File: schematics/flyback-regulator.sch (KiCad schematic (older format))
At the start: 24 parts

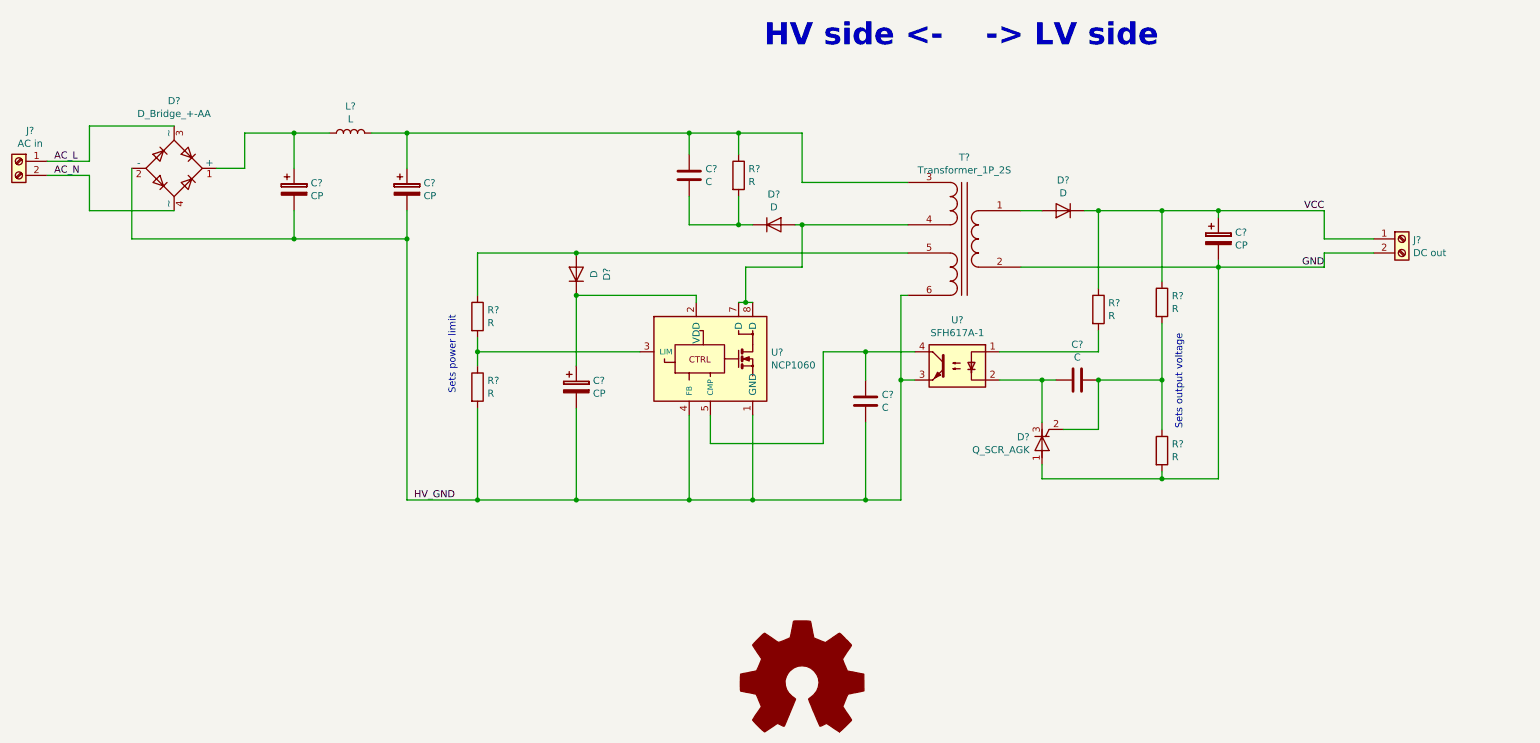
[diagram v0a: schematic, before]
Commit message: [sch] Edited to NCP1251
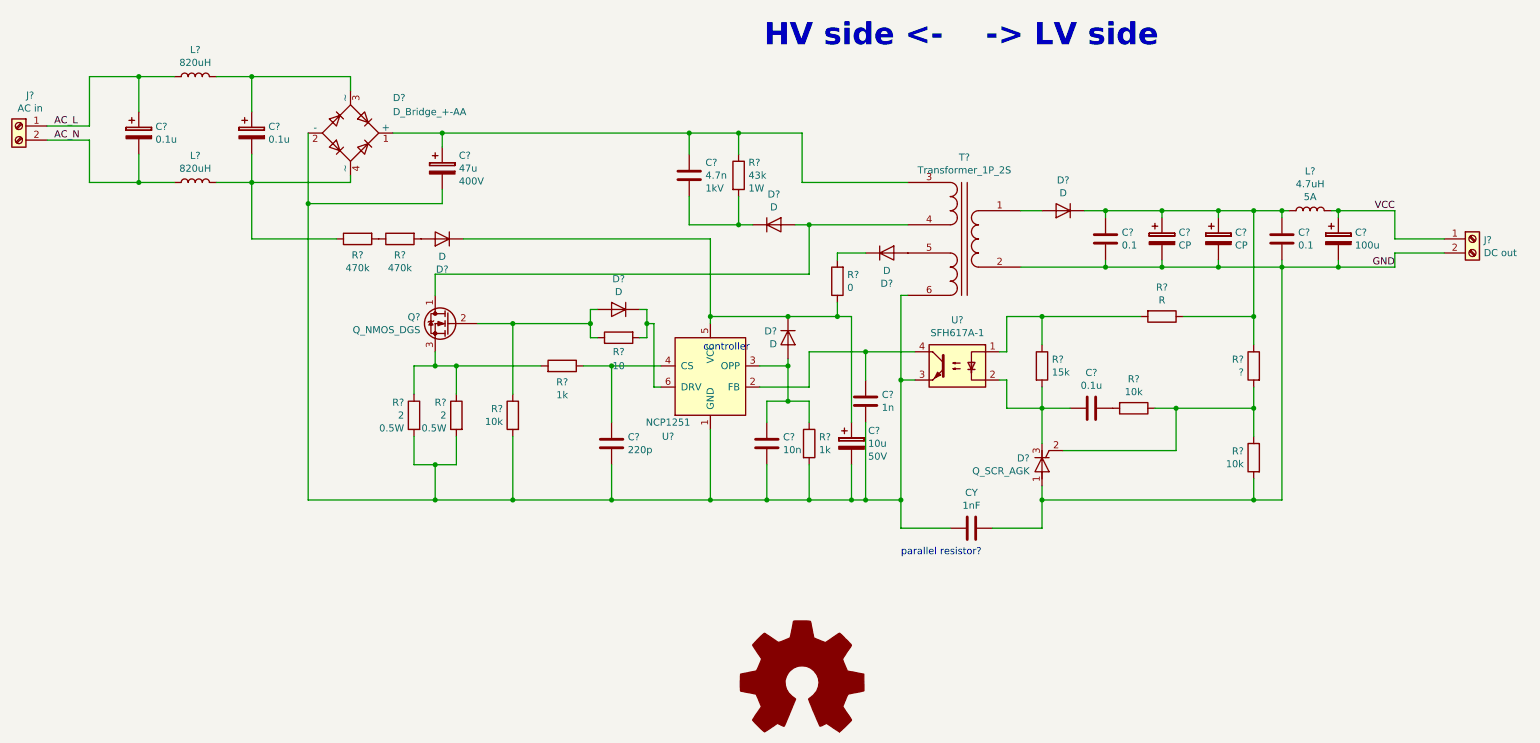
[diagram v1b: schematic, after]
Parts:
- removed C?: CP, symbol Device:CP
- removed R? (x4): R, symbol Device:R
- removed U?: NCP1060, Package_DIP:PowerIntegrations_PDIP-8B, symbol flyback-regulator-dedicated:NCP1060
- added C?: 47u, symbol Device:CP
- added C? (x2): 0.1, symbol Device:C
- added C?: CP, symbol Device:CP
- added C?: 100u, symbol Device:CP
- added C?: 10n, symbol Device:C
- added C?: 10u, symbol Device:CP
- added C?: 220p, symbol Device:C
- added CY: 1nF, symbol Device:C
- added D? (x3): D, symbol Device:D
- added L?: 820uH, symbol Device:L
- added L?: 4.7uH, symbol Device:L
- added Q?: Q_NMOS_DGS, symbol Device:Q_NMOS_DGS
- added R? (x2): 2, symbol Device:R
- added R? (x2): 10k, symbol Device:R
- added R?: 10, symbol Device:R
- added R? (x2): 470k, symbol Device:R
- added R?: R, symbol Device:R
- added R?: 15k, symbol Device:R
- added R?: ?, symbol Device:R
- added R? (x2): 1k, symbol Device:R
- added R?: 0, symbol Device:R
- added U?: NCP1251, symbol flyback-regulator-dedicated:NCP1251
- C? (x2): value CP -> 0.1u
- C?: value C -> 0.1u
- C?: value C -> 4.7n; Voltage (none) -> 1kV
- C?: value C -> 1n
- L?: value L -> 820uH
- R?: value R -> 10k
- R?: value R -> 43k; Power (none) -> 1W
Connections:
- net AC_L: now also C?.1, L?.1; no longer D?.3 (~~)
- net AC_N: now also C?.2, L?.1; no longer D?.4 (~~)
- net GND: now also C?.2, C?.2, C?.2, C?.2, CY.2, R?.2; no longer R?.2
- net VCC: now also C?.1, L?.2; no longer C?.1, D?.1 (K)
- net at C?.2, R?.1, T?.3 (SA): now also D?.1 (+), C?.1; no longer C?.1, L?.2
- net at D?.2 (A), T?.4 (SB): now also Q?.1 (D)
- net at U?.1: now also R?.1, R?.2
- net at C?.1, D?.3 (K), U?.2: now also R?.2
- net at C?.2, U?.4: now also U?.2 (FB)
- net at D?.2 (G), R?.1: now also R?.1, R?.2; no longer C?.2
- net at D?.1 (K): now also R?.2
- net HV_GND: no longer names the net of C?.1, D?.2 (-), T?.6 (SD), U?.3
- net HV_GND: now also C?.1, C?.1, C?.2, C?.2, CY.1, R?.2, R?.2, R?.2, R?.2, U?.1 (GND); no longer C?.2, C?.2
- new net: C?.1, D?.3 (~~), L?.2
- new net: C?.2, D?.4 (~~), L?.2, R?.1
- new net: C?.1, C?.1, C?.1, C?.1, D?.1 (K), L?.1, R?.1, R?.1
- new net: C?.2, R?.2
- new net: D?.2 (A), Q?.2 (G), R?.1, R?.1
- new net: Q?.3 (S), R?.1, R?.1, R?.2
- new net: D?.1 (K), R?.2, U?.6 (DRV)
- new net: R?.1, R?.2
- new net: D?.2 (A), R?.2
- new net: C?.1, D?.1 (K), D?.1 (K), R?.1, U?.5 (VCC)
- new net: C?.2, D?.2 (A), R?.1, U?.3 (OPP)
- new net: C?.2, R?.1, U?.4 (CS)
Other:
- note added: "controller"
- note added: "parallel resistor?"
- note removed: "Sets output voltage"
- note removed: "Sets power limit"
- moved on the sheet: C?, D?, J?, L?, R?
